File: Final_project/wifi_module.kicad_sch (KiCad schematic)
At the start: 12 parts, among them U4 ESP32-WROOM-32

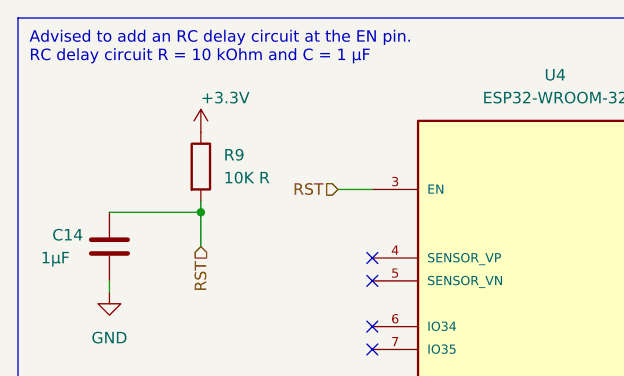
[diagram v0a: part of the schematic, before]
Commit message: Fix 3V3 label, fix USB footprint, layout begin
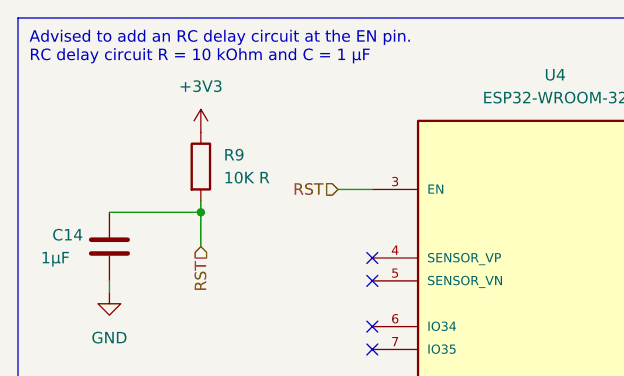
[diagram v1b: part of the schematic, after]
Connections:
- net +3.3V is gone; now on net +3V3: R9.1
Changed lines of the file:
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@@
     (effects (font (size 1.27 1.27)) (justify right))
-  )
-  (symbol (lib_id "power:+3.3V") (at 35.56 26.67 0) (unit 1)
-    (in_bom yes) (on_board yes)
-    (property "Reference" "#PWR0136" (id 0) (at 35.56 30.48 0)
-      (effects (font (size 1.27 1.27)) hide)
-    )
-    (property "Value" "+3.3V" (id 1) (at 35.5601 22.86 0)
-      (effects (font (size 1.27 1.27)) (justify left))
-    )
-    (property "Footprint" "" (id 2) (at 35.56 26.67 0)
-      (effects (font (size 1.27 1.27)) hide)
-    )
-    (property "Datasheet" "" (id 3) (at 35.56 26.67 0)
-      (effects (font (size 1.27 1.27)) hide)
-    )
-    (pin "1")
   )
   (symbol (lib_id "ESP32-WROOM-32:ESP32-WROOM-32") (at 74.93 60.96 0) (unit 1)
@@
       (effects (font (size 1.27 1.27)) hide)
     )
+    (pin "1")
+  )
+  (symbol (lib_id "power:+3V3") (at 35.56 26.67 0) (unit 1)
+    (in_bom yes) (on_board yes) (fields_autoplaced)
+    (property "Reference" "#PWR0136" (id 0) (at 35.56 30.48 0)
+      (effects (font (size 1.27 1.27)) hide)
+    )
+    (property "Value" "+3V3" (id 1) (at 35.56 21.59 0))
+    (property "Footprint" "" (id 2) (at 35.56 26.67 0)
+      (effects (font (size 1.27 1.27)) hide)
+    )
+    (property "Datasheet" "" (id 3) (at 35.56 26.67 0)
+      (effects (font (size 1.27 1.27)) hide)
+    )

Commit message: almost finished layout
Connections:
- net +3V3: no longer R9.1
- new net +3.3V: R9.1
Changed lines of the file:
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@@
     (effects (font (size 1.27 1.27)) (justify right))
+  )
+  (symbol (lib_id "power:+3.3V") (at 35.56 26.67 0) (unit 1)
+    (in_bom yes) (on_board yes)
+    (property "Reference" "#PWR0136" (id 0) (at 35.56 30.48 0)
+      (effects (font (size 1.27 1.27)) hide)
+    )
+    (property "Value" "+3.3V" (id 1) (at 35.5601 22.86 0)
+      (effects (font (size 1.27 1.27)) (justify left))
+    )
+    (property "Footprint" "" (id 2) (at 35.56 26.67 0)
+      (effects (font (size 1.27 1.27)) hide)
+    )
+    (property "Datasheet" "" (id 3) (at 35.56 26.67 0)
+      (effects (font (size 1.27 1.27)) hide)
+    )
+    (pin "1")
   )
   (symbol (lib_id "ESP32-WROOM-32:ESP32-WROOM-32") (at 74.93 60.96 0) (unit 1)
@@
       (effects (font (size 1.27 1.27)) hide)
     )
-    (pin "1")
-  )
-  (symbol (lib_id "power:+3V3") (at 35.56 26.67 0) (unit 1)
-    (in_bom yes) (on_board yes) (fields_autoplaced)
-    (property "Reference" "#PWR0136" (id 0) (at 35.56 30.48 0)
-      (effects (font (size 1.27 1.27)) hide)
-    )
-    (property "Value" "+3V3" (id 1) (at 35.56 21.59 0))
-    (property "Footprint" "" (id 2) (at 35.56 26.67 0)
-      (effects (font (size 1.27 1.27)) hide)
-    )
-    (property "Datasheet" "" (id 3) (at 35.56 26.67 0)
-      (effects (font (size 1.27 1.27)) hide)
-    )
